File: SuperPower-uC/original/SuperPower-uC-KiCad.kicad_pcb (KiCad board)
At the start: 2 copper layers, 95 x 42 mm, 168 parts, among them J1 JST_PH_S2B_thru, J2 Barrel_Jack_Switch, J3 Conn_01x02_Male, J4 DNP/JST_ZH_S2B_thru, J5 JST_XH_S2B_thru, J6 Conn_01x02_Male, J7 mcu_pinout, J8 mcu_pinout, Q1 DMN2019UTS, Q10 2N7002A, Q11 2N7002A, Q12 DMP2035UVT, Q13 DMP2035UVT, Q14 DMP2035UVT, Q2 DMP3028LSD, Q3 DMN3018SSD, Q4 2N7002A, Q5 DMP2035UVT, Q6 BSS84-7-F, Q7 S8050, Q8 S8050, Q9 2N7002A, SW1 DNP/SKRKAEE020, U1 AP9101CK6-AYTRG1, U10 TPS63070RNMT, U2 USB-C, U3 IP4220CZ6, U4 LTC4162EUFD-LAD, U5 RV-3028-C7, U6 CP2102N-A01-GQFN28, U7 ESP32-WROOM32, U8 TPS70933DRVT, U9 TPS63070RNMT

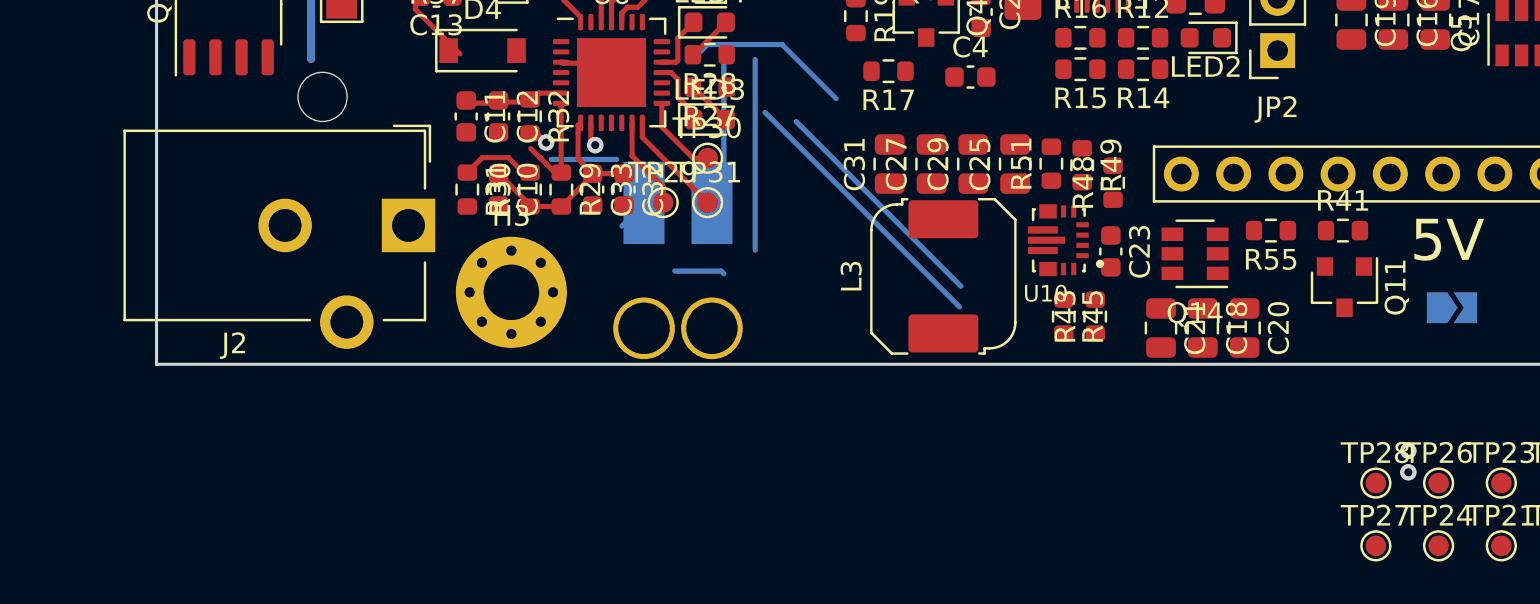
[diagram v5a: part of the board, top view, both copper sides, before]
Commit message: Update DC Power Jack connector
Add 3D Model
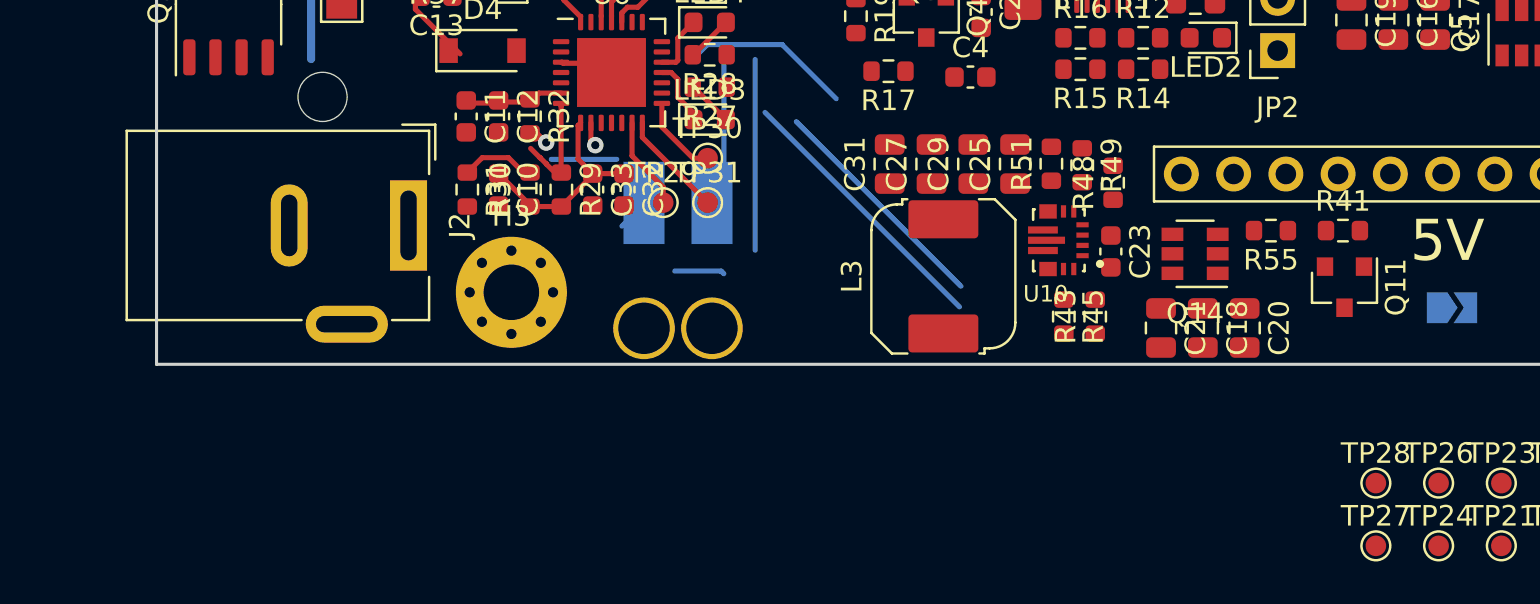
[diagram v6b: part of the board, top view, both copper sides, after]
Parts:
- J2: footprint Connector_BarrelJack:BarrelJack_CUI_PJ-102AH_Horizontal -> Connector_BarrelJack:BarrelJack_Wuerth_6941xx301002
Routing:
- net /MCU Module/TXD: vias 1 -> 0
- net /MCU Module/RXD: vias 1 -> 0

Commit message: Add JST ZH 3D Model
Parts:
- J4: footprint Connector_JST_user:JST_ZH_S2B-ZR_1x02_P1.50mm_Horizontal -> JST_ZH_S2B_THRU:JST_ZH_S2B-ZR_1x02_P1.50mm_Horizontal

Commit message: Update DMP3028LSD SO-8 3D Package
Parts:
- Q2: footprint Package_SO:SO-8_3.9x4.9mm_P1.27mm -> DMP3028LSD:SO-8_3.9x4.9mm_P1.27mm
